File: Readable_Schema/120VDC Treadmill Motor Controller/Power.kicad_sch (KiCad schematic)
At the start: 22 parts, among them J1 TB005-762-03BE, J6 TB0011-350-03BE, J7 OSTT7020150, K1 T9GV1L14-24, Q5 IPP60R060P7XKSA1, U5 TPSI3050QDWZRQ1, U8 RAC05E-05SKT

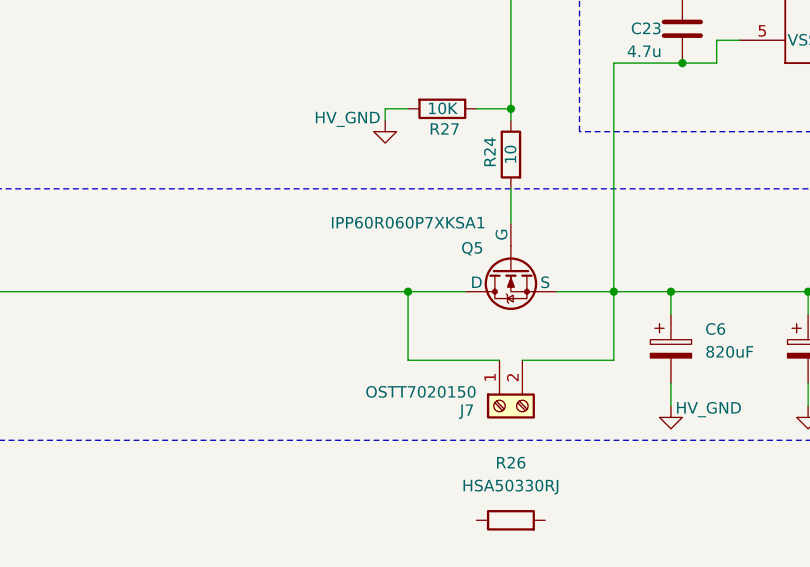
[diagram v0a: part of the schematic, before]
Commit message: -Updated kicad fet symbol to swap gate and drain numbers to match the datasheet
-There are not vertically mounted rectifier alternatives that are capable of 50 amps so stuck with the current one
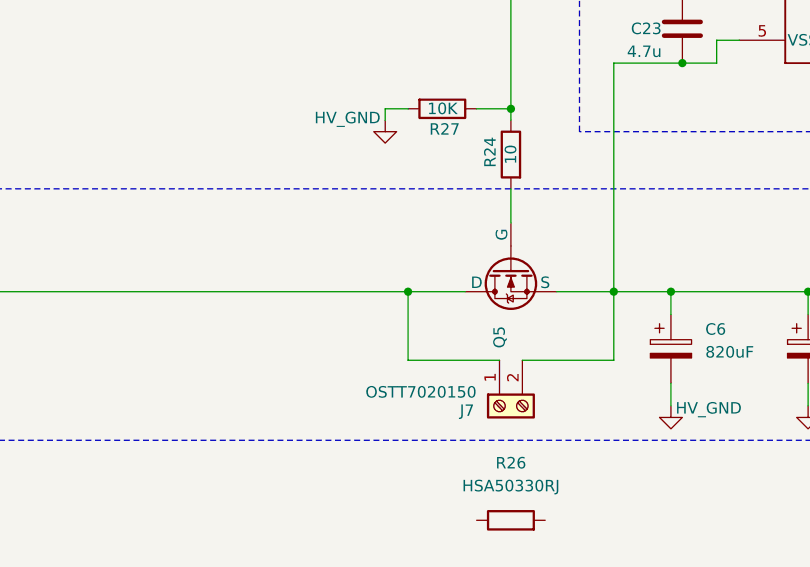
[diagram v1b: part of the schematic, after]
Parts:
- removed Q5: IPP60R060P7XKSA1, Package_TO_SOT_THT:TO-220-3_Vertical, symbol Simulation_SPICE:NMOS
- added Q5: IPP60R060P7XKSA1, Package_TO_SOT_THT:TO-220-3_Vertical, symbol Treadmill_Comp:IPP60R060P7XKSA1
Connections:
- net 170V Rect: now also Q5.3 (S)
- net at R24.2: now also Q5.1 (G)
- net at D1.1 (+), J7.1 (Pin_1): now also Q5.2 (D)
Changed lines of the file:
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@@
+	)
+	(symbol
+		(lib_id "Treadmill_Comp:IPP60R060P7XKSA1")
+		(at 172.72 87.63 90)
+		(mirror x)
+		(unit 1)
+		(exclude_from_sim no)
+		(in_bom yes)
+		(on_board yes)
+		(dnp no)
+		(property "Reference" "Q5"
+			(at 171.4499 93.98 0)
+			(effects
+				(font
+					(size 1.27 1.27)
+				)
+				(justify left)
+			)
+		)
+		(property "Value" "IPP60R060P7XKSA1"
+			(at 173.9899 93.98 0)
+			(effects
+				(font
+					(size 1.27 1.27)
+				)
+				(justify left)
+				(hide yes)
+			)
+		)
+		(property "Footprint" "Package_TO_SOT_THT:TO-220-3_Vertical"
+			(at 170.18 92.71 0)
+			(effects
+				(font
+					(size 1.27 1.27)
+				)
+				(hide yes)
+			)
+		)
+		(property "Datasheet" "https://www.infineon.com/dgdl/Infineon-IPP60R060P7-DS-v02_00-EN.pdf?fileId=5546d4625acbae4c015accdf20660227"
+			(at 185.42 87.63 0)
+			(effects
+				(font
+					(size 1.27 1.27)
+				)
+				(hide yes)
+			)
+		)
+		(property "Description" "N-MOSFET transistor, drain/source/gate"
+			(at 172.72 87.63 0)
+			(effects
+				(font
+					(size 1.27 1.27)
+				)
+				(hide yes)
+			)
+		)
+		(property "Sim.Device" "NMOS"
+			(at 189.865 87.63 0)
+			(effects
+				(font
+					(size 1.27 1.27)
+				)
+				(hide yes)
+			)
+		)
+		(property "Sim.Type" "VDMOS"
+			(at 191.77 87.63 0)
+			(effects
+				(font
+					(size 1.27 1.27)
+				)
+				(hide yes)
+			)
+		)
+		(property "Sim.Pins" "1=D 2=G 3=S"
+			(at 187.96 87.63 0)
+			(effects
+				(font
+					(size 1.27 1.27)
+				)
+				(hide yes)
+			)
+		)
+		(pin "2"
+		)
+		(pin "1"
+		)
+		(pin "3"
+		)
+		(instances
+			(project "120VDC Treadmill Motor Controller"
+				(path "/319bc5c0-2dd5-4df3-a34b-9170833ebccd/1fa0373b-ff98-4bf0-acad-d32450f2dcd0"
+					(reference "Q5")
+					(unit 1)
+				)
+			)
+		)
 	)
 	(symbol
@@
 					(unit 1)
 				)
-			)
-		)
-	)
-	(symbol
-		(lib_id "Simulation_SPICE:NMOS")
-		(at 172.72 87.63 90)
-		(mirror x)
-		(unit 1)
-		(exclude_from_sim no)
-		(in_bom yes)
-		(on_board yes)
-		(dnp no)
-		(property "Reference" "Q5"
-			(at 169.672 85.344 90)
-			(effects
-				(font
-					(size 1.27 1.27)
-				)
-				(justify left)
-			)
-		)
-		(property "Value" "IPP60R060P7XKSA1"
-			(at 169.926 82.55 90)
-			(effects
-				(font
-					(size 1.27 1.27)
-				)
-				(justify left)
-			)
-		)
-		(property "Footprint" "Package_TO_SOT_THT:TO-220-3_Vertical"
-			(at 170.18 92.71 0)
-			(effects
-				(font
-					(size 1.27 1.27)
-				)
-				(hide yes)
-			)
-		)
-		(property "Datasheet" "https://www.infineon.com/dgdl/Infineon-IPP60R060P7-DS-v02_00-EN.pdf?fileId=5546d4625acbae4c015accdf20660227"
-			(at 185.42 87.63 0)
-			(effects
-				(font
-					(size 1.27 1.27)
-				)
-				(hide yes)
-			)
-		)
-		(property "Description" "N-MOSFET transistor, drain/source/gate"
-			(at 172.72 87.63 0)
-			(effects
-				(font
-					(size 1.27 1.27)
-				)
-				(hide yes)
-			)
-		)
-		(property "Sim.Device" "NMOS"
-			(at 189.865 87.63 0)
-			(effects
-				(font
-					(size 1.27 1.27)
-				)
-				(hide yes)
-			)
-		)
-		(property "Sim.Type" "VDMOS"
-			(at 191.77 87.63 0)
-			(effects
-				(font
-					(size 1.27 1.27)
-				)
-				(hide yes)
-			)
-		)
-		(property "Sim.Pins" "1=D 2=G 3=S"
-			(at 187.96 87.63 0)
-			(effects
-				(font
-					(size 1.27 1.27)
-				)
-				(hide yes)
-			)
-		)
-		(pin "2"
-		)
-		(pin "3"
-		)
-		(pin "1"
-		)
-		(instances
-			(project "120VDC Treadmill Motor Controller"
-				(path "/319bc5c0-2dd5-4df3-a34b-9170833ebccd/1fa0373b-ff98-4bf0-acad-d32450f2dcd0"
-					(reference "Q5")
-					(unit 1)
-				)

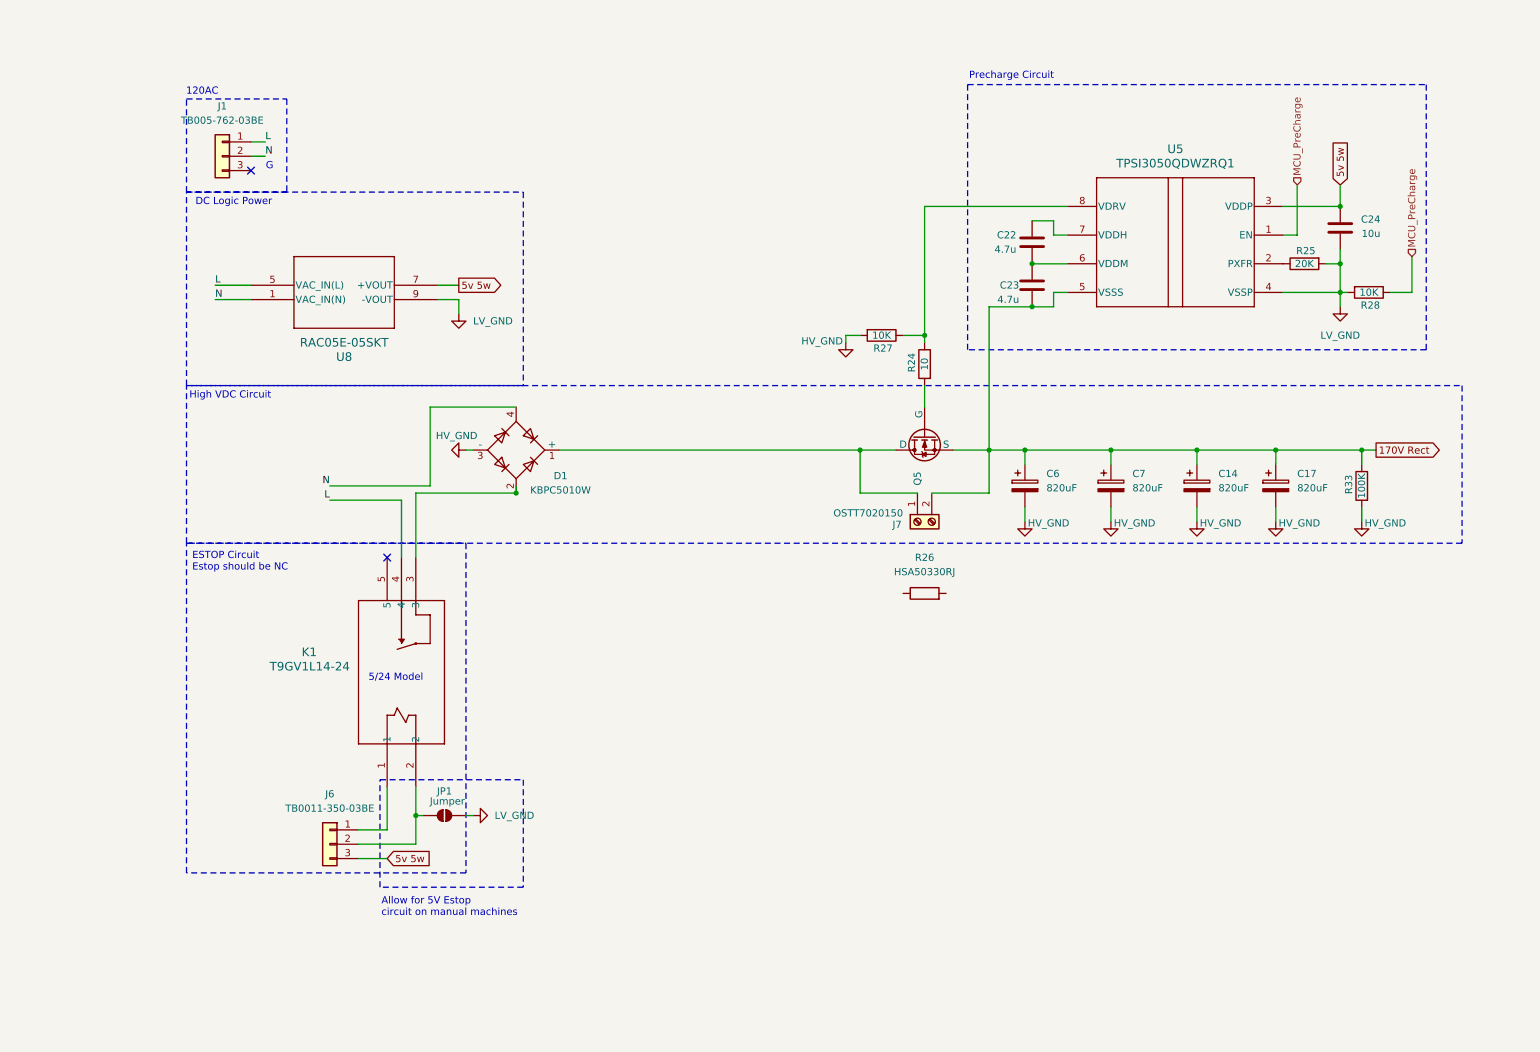
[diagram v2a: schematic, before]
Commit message: -Added voltage sense
-Need to add some kind of LED to tell that the board is HOT

-Need to work with ross to understand the DNMOS setup
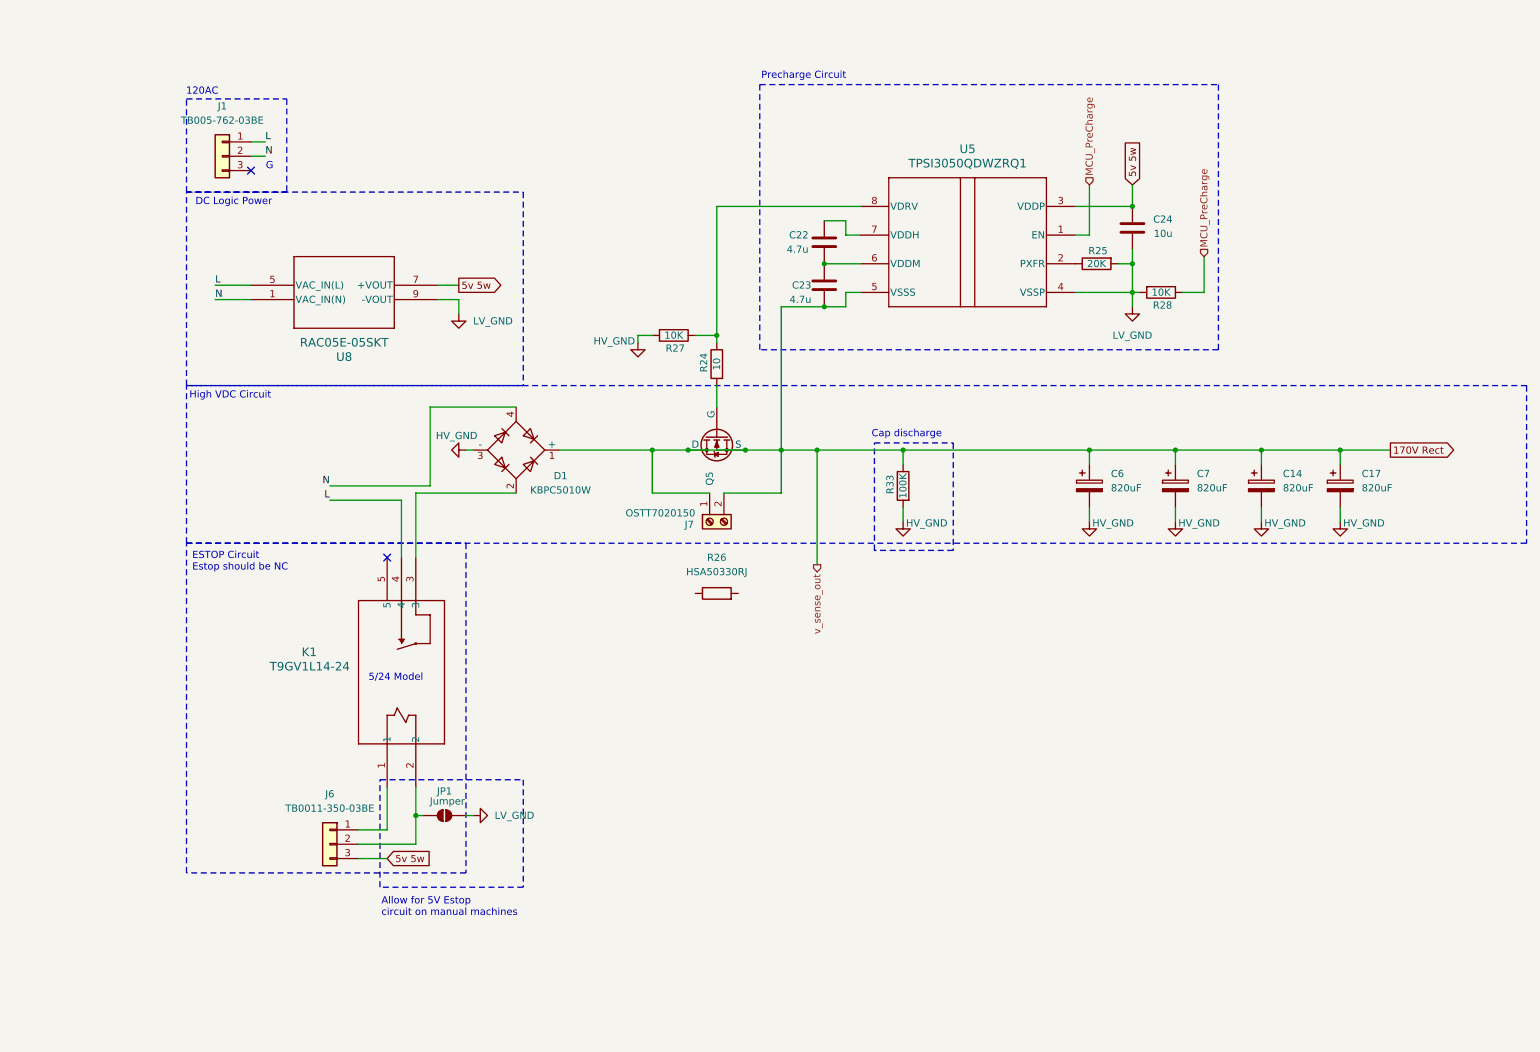
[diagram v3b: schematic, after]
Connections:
- net 170V Rect: now also D1.1 (+), J7.1 (Pin_1), Q5.2 (D)
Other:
- note added: "Cap discharge"
- moved on the sheet: C14, C17, C22, C23, C24, C6, C7, J7, Q5, R24, R25, R26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

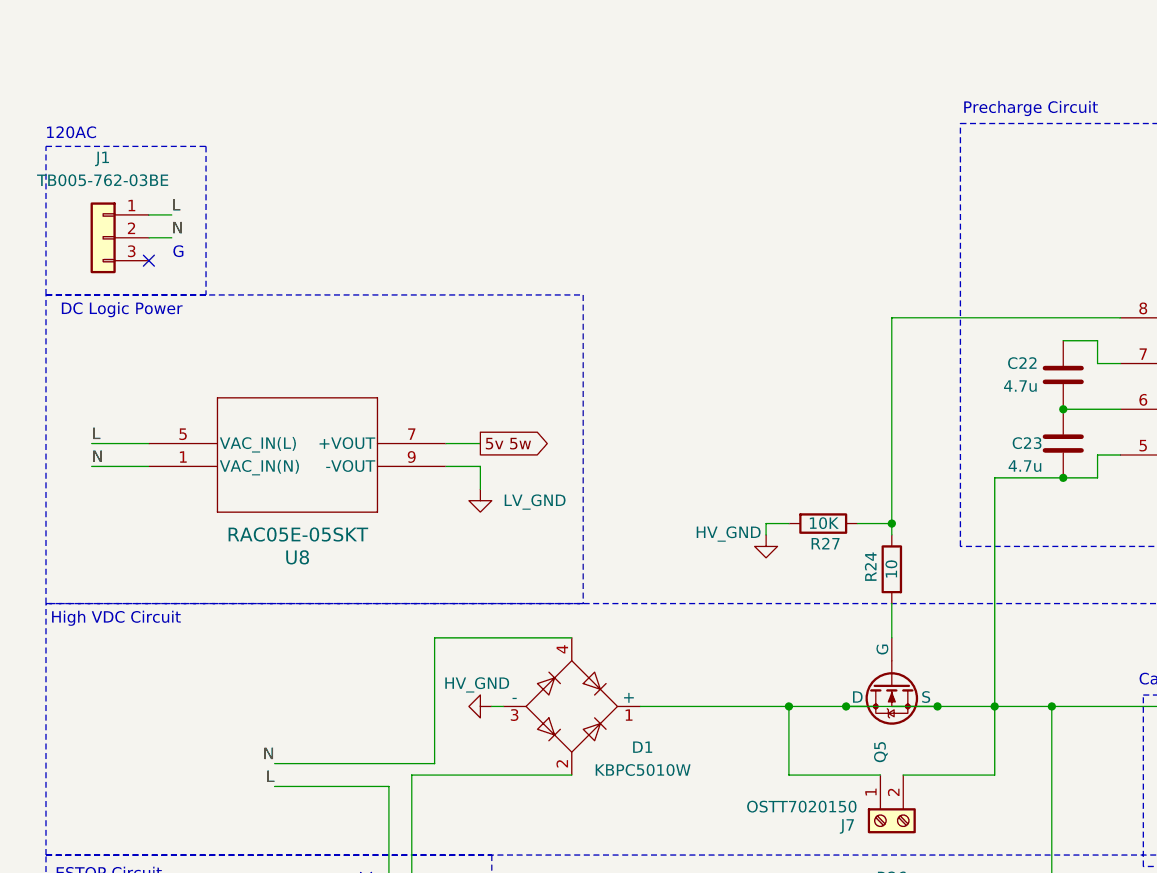
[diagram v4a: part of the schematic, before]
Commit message: -Basically realized that we need to redo the whole power structure
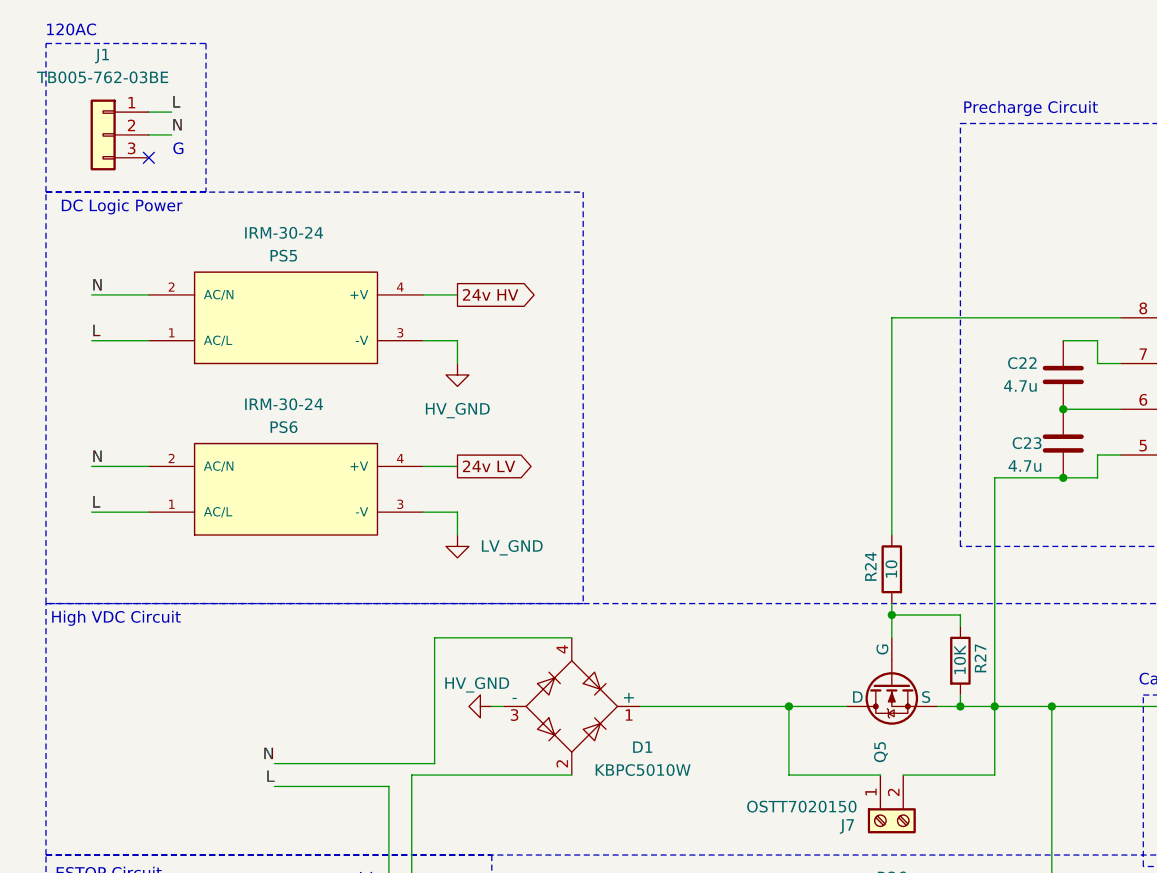
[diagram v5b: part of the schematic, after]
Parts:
- removed U8: RAC05E-05SKT, Treadmill_Feet:RAC05E-KT_RCP, symbol Treadmill_Comp:RAC05E-05SKT
- added PS5, PS6: IRM-30-24, Treadmill_Feet:CONV_IRM-30-24, symbol Treadmill_Comp:IRM-30-24
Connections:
- net 170V Rect: now also R27.2; no longer D1.1 (+), J7.1 (Pin_1), Q5.2 (D)
- net HV_GND: now also PS5.3 (-V); no longer R27.2
- net L: now also PS5.1 (AC/L), PS6.1 (AC/L)
- net LV_GND: now also PS6.3 (-V)
- net N: now also PS5.2 (AC/N), PS6.2 (AC/N)
- net at R24.1, U5.8 (VDRV): no longer R27.1
- net at Q5.1 (G), R24.2: now also R27.1
- new net: D1.1 (+), J7.1 (Pin_1), Q5.2 (D)
- new net 24v HV: PS5.4 (+V)
- new net 24v LV: PS6.4 (+V)
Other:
- moved on the sheet: J1, R27
